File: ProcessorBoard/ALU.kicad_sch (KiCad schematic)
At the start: 2 parts, among them U43 IDT7381

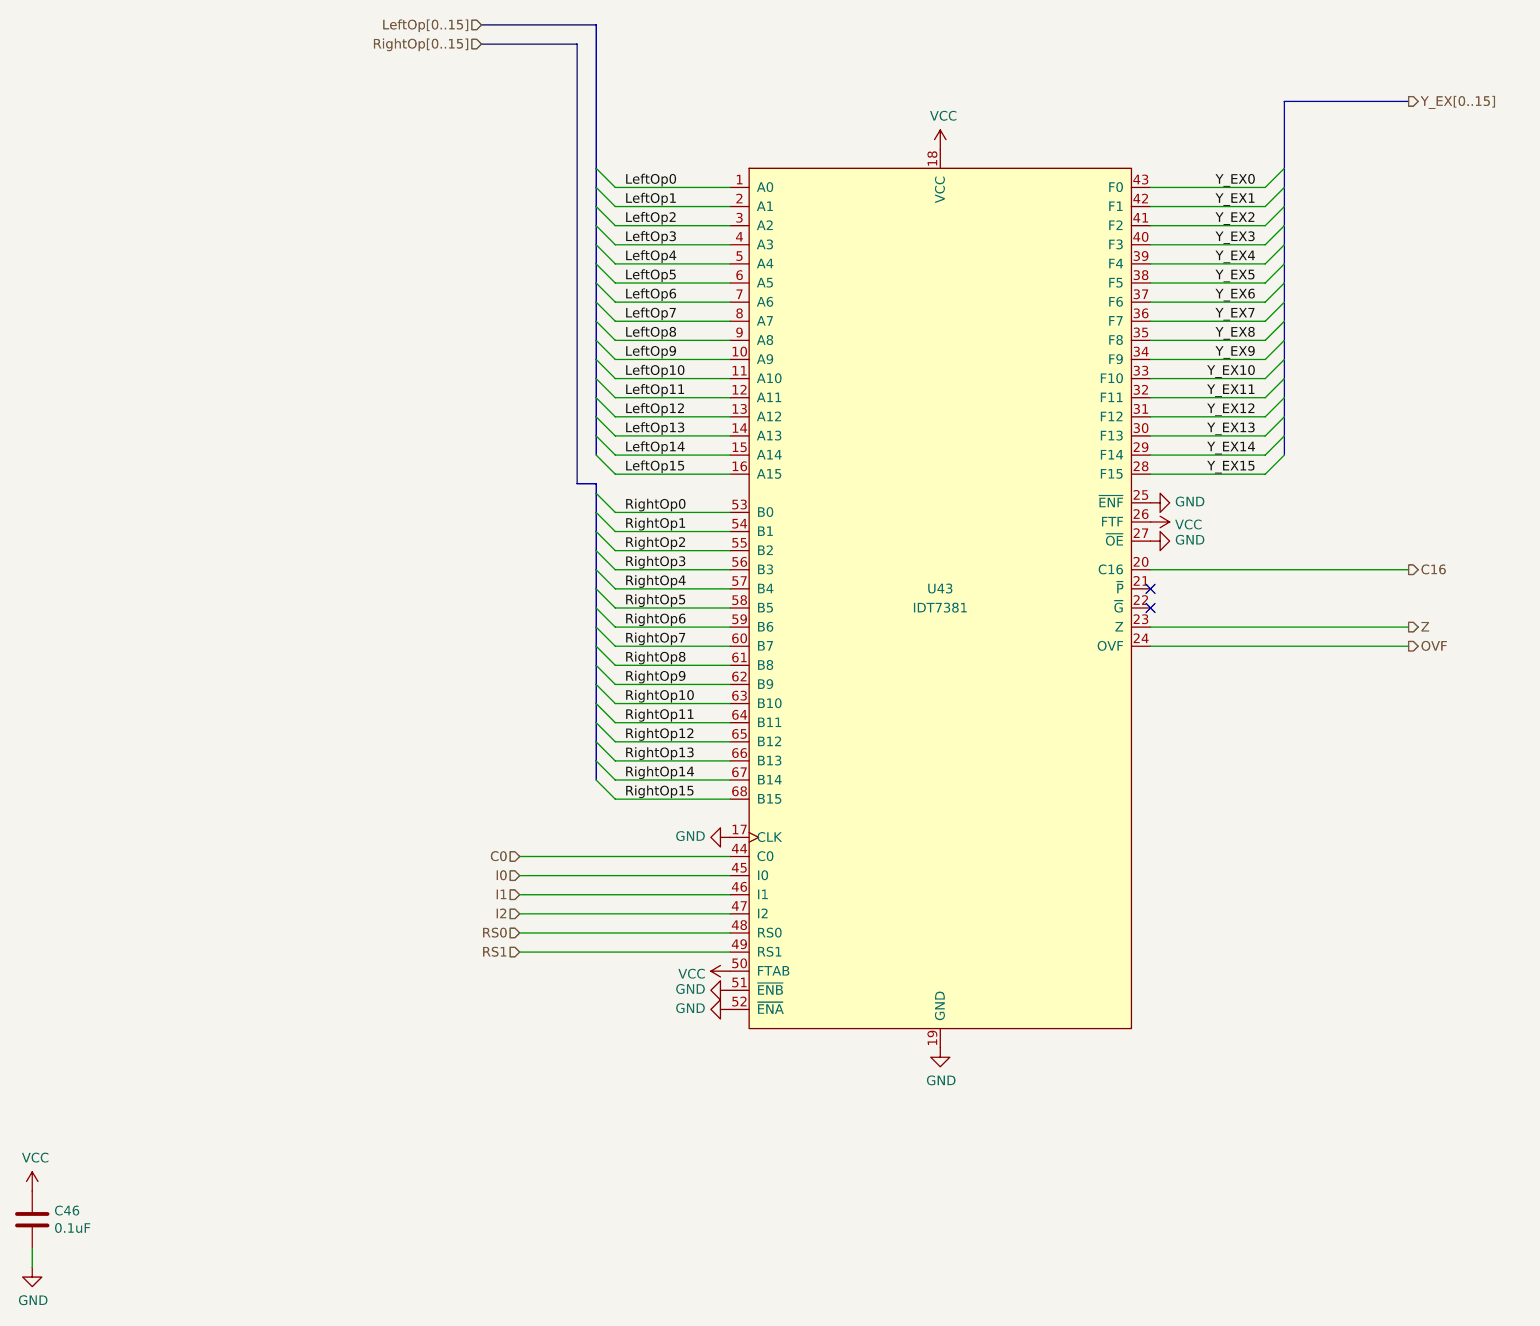
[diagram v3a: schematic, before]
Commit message: ProcessorBoard: Replace Instruction ROM with a header for a daughter board
ROMs will be relocated to a daughter board to allow the memories and their
sockets to be swapped easily.
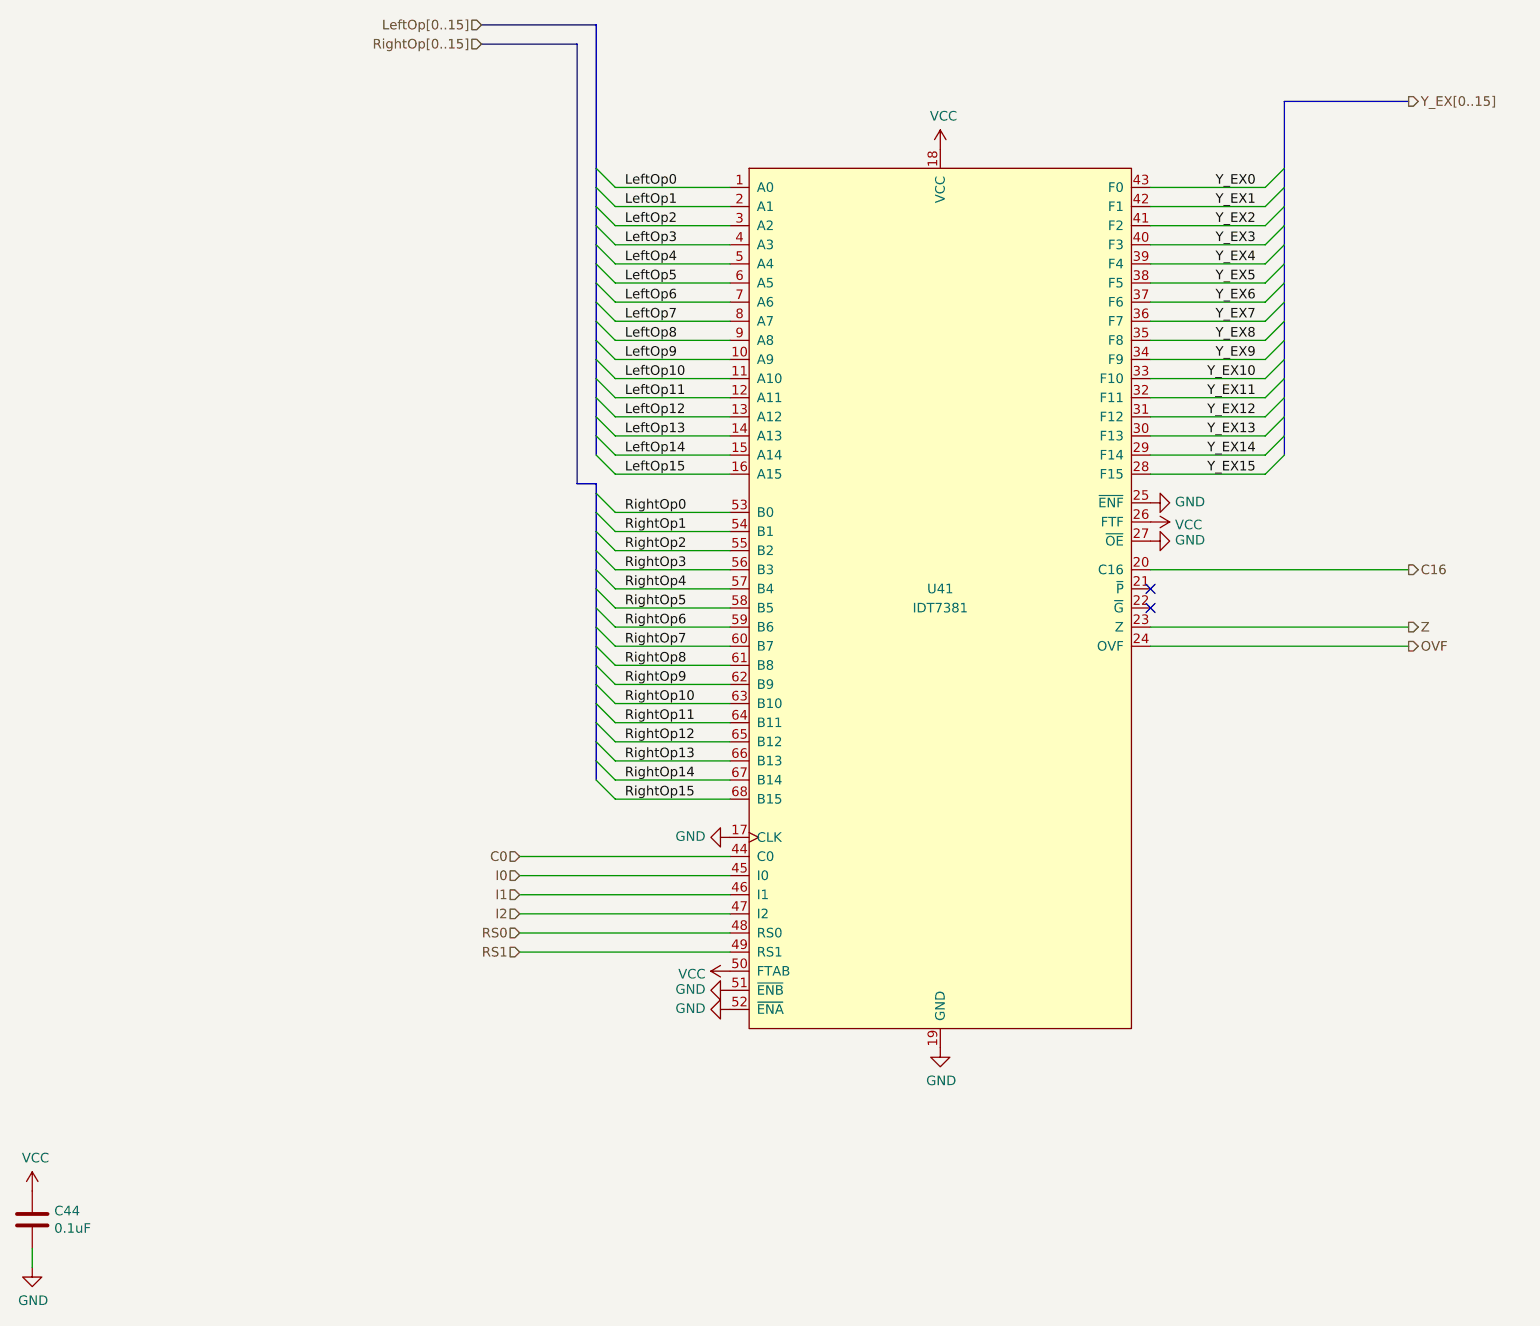
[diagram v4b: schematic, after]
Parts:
- renumbered C46 to C44, U43 to U41
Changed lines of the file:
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@@
   (symbol (lib_id "Device:C") (at 21.59 185.42 0) (unit 1)
     (in_bom yes) (on_board yes) (dnp no)
-    (property "Reference" "C46" (at 24.511 184.2516 0)
+    (property "Reference" "C44" (at 24.511 184.2516 0)
       (effects (font (size 1.27 1.27)) (justify left))
     )
@@
       (project "ProcessorBoard"
         (path "/83c5181e-f5ee-453c-ae5c-d7256ba8837d/00000000-0000-0000-0000-000060a71bbf/00000000-0000-0000-0000-00005fc6fe4b"
-          (reference "C46") (unit 1)
+          (reference "C44") (unit 1)
         )
       )
@@
   (symbol (lib_id "power:VCC") (at 21.59 181.61 0) (unit 1)
     (in_bom yes) (on_board yes) (dnp no)
-    (property "Reference" "#PWR0293" (at 21.59 185.42 0)
+    (property "Reference" "#PWR0285" (at 21.59 185.42 0)
       (effects (font (size 1.27 1.27)) hide)
     )
@@
       (project "ProcessorBoard"
         (path "/83c5181e-f5ee-453c-ae5c-d7256ba8837d/00000000-0000-0000-0000-000060a71bbf/00000000-0000-0000-0000-00005fc6fe4b"
-          (reference "#PWR0293") (unit 1)
+          (reference "#PWR0285") (unit 1)
         )
       )
@@
   (symbol (lib_id "power:GND") (at 21.59 191.77 0) (unit 1)
     (in_bom yes) (on_board yes) (dnp no)
-    (property "Reference" "#PWR0294" (at 21.59 198.12 0)
+    (property "Reference" "#PWR0286" (at 21.59 198.12 0)
       (effects (font (size 1.27 1.27)) hide)
     )
@@
       (project "ProcessorBoard"
         (path "/83c5181e-f5ee-453c-ae5c-d7256ba8837d/00000000-0000-0000-0000-000060a71bbf/00000000-0000-0000-0000-00005fc6fe4b"
-          (reference "#PWR0294") (unit 1)
+          (reference "#PWR0286") (unit 1)
         )
       )
@@
   (symbol (lib_id "EXModule-rescue:IDT7381-CPU") (at 142.24 102.87 0) (unit 1)
     (in_bom yes) (on_board yes) (dnp no)
-    (property "Reference" "U43" (at 142.24 101.6 0)
+    (property "Reference" "U41" (at 142.24 101.6 0)
       (effects (font (size 1.27 1.27)))
     )
@@
       (project "ProcessorBoard"
         (path "/83c5181e-f5ee-453c-ae5c-d7256ba8837d/00000000-0000-0000-0000-000060a71bbf/00000000-0000-0000-0000-00005fc6fe4b"
-          (reference "U43") (unit 1)
+          (reference "U41") (unit 1)
         )
       )
@@
   (symbol (lib_id "power:VCC") (at 142.24 43.18 0) (unit 1)
     (in_bom yes) (on_board yes) (dnp no)
-    (property "Reference" "#PWR0299" (at 142.24 46.99 0)
+    (property "Reference" "#PWR0291" (at 142.24 46.99 0)
       (effects (font (size 1.27 1.27)) hide)
     )
@@
       (project "ProcessorBoard"
         (path "/83c5181e-f5ee-453c-ae5c-d7256ba8837d/00000000-0000-0000-0000-000060a71bbf/00000000-0000-0000-0000-00005fc6fe4b"
-          (reference "#PWR0299") (unit 1)
+          (reference "#PWR0291") (unit 1)
         )
       )
@@
   (symbol (lib_id "power:GND") (at 142.24 162.56 0) (unit 1)
     (in_bom yes) (on_board yes) (dnp no)
-    (property "Reference" "#PWR0300" (at 142.24 168.91 0)
+    (property "Reference" "#PWR0292" (at 142.24 168.91 0)
       (effects (font (size 1.27 1.27)) hide)
     )
@@
       (project "ProcessorBoard"
         (path "/83c5181e-f5ee-453c-ae5c-d7256ba8837d/00000000-0000-0000-0000-000060a71bbf/00000000-0000-0000-0000-00005fc6fe4b"
-          (reference "#PWR0300") (unit 1)
+          (reference "#PWR0292") (unit 1)
         )
       )
@@
   (symbol (lib_id "power:GND") (at 170.18 90.17 90) (unit 1)
     (in_bom yes) (on_board yes) (dnp no)
-    (property "Reference" "#PWR0301" (at 176.53 90.17 0)
+    (property "Reference" "#PWR0293" (at 176.53 90.17 0)
       (effects (font (size 1.27 1.27)) hide)
     )
@@
       (project "ProcessorBoard"
         (path "/83c5181e-f5ee-453c-ae5c-d7256ba8837d/00000000-0000-0000-0000-000060a71bbf/00000000-0000-0000-0000-00005fc6fe4b"
-          (reference "#PWR0301") (unit 1)
+          (reference "#PWR0293") (unit 1)
         )
       )
@@
   (symbol (lib_id "power:GND") (at 114.3 154.94 270) (mirror x) (unit 1)
     (in_bom yes) (on_board yes) (dnp no)
-    (property "Reference" "#PWR0297" (at 107.95 154.94 0)
+    (property "Reference" "#PWR0289" (at 107.95 154.94 0)
       (effects (font (size 1.27 1.27)) hide)
     )
@@
       (project "ProcessorBoard"
         (path "/83c5181e-f5ee-453c-ae5c-d7256ba8837d/00000000-0000-0000-0000-000060a71bbf/00000000-0000-0000-0000-00005fc6fe4b"
-          (reference "#PWR0297") (unit 1)
+          (reference "#PWR0289") (unit 1)
         )
       )
@@
   (symbol (lib_id "power:GND") (at 114.3 157.48 270) (mirror x) (unit 1)
     (in_bom yes) (on_board yes) (dnp no)
-    (property "Reference" "#PWR0298" (at 107.95 157.48 0)
+    (property "Reference" "#PWR0290" (at 107.95 157.48 0)
       (effects (font (size 1.27 1.27)) hide)
     )
@@
       (project "ProcessorBoard"
         (path "/83c5181e-f5ee-453c-ae5c-d7256ba8837d/00000000-0000-0000-0000-000060a71bbf/00000000-0000-0000-0000-00005fc6fe4b"
-          (reference "#PWR0298") (unit 1)
+          (reference "#PWR0290") (unit 1)
         )
       )
@@
   (symbol (lib_id "power:VCC") (at 170.18 92.71 270) (unit 1)
     (in_bom yes) (on_board yes) (dnp no)
-    (property "Reference" "#PWR0302" (at 166.37 92.71 0)
+    (property "Reference" "#PWR0294" (at 166.37 92.71 0)
       (effects (font (size 1.27 1.27)) hide)
     )
@@
       (project "ProcessorBoard"
         (path "/83c5181e-f5ee-453c-ae5c-d7256ba8837d/00000000-0000-0000-0000-000060a71bbf/00000000-0000-0000-0000-00005fc6fe4b"
-          (reference "#PWR0302") (unit 1)
+          (reference "#PWR0294") (unit 1)
         )
       )
@@
   (symbol (lib_id "power:GND") (at 114.3 134.62 270) (mirror x) (unit 1)
     (in_bom yes) (on_board yes) (dnp no)
-    (property "Reference" "#PWR0295" (at 107.95 134.62 0)
+    (property "Reference" "#PWR0287" (at 107.95 134.62 0)
       (effects (font (size 1.27 1.27)) hide)
     )
@@
       (project "ProcessorBoard"
         (path "/83c5181e-f5ee-453c-ae5c-d7256ba8837d/00000000-0000-0000-0000-000060a71bbf/00000000-0000-0000-0000-00005fc6fe4b"
-          (reference "#PWR0295") (unit 1)
+          (reference "#PWR0287") (unit 1)
         )
       )
@@
   (symbol (lib_id "power:VCC") (at 114.3 152.4 90) (mirror x) (unit 1)
     (in_bom yes) (on_board yes) (dnp no)
-    (property "Reference" "#PWR0296" (at 118.11 152.4 0)
+    (property "Reference" "#PWR0288" (at 118.11 152.4 0)
       (effects (font (size 1.27 1.27)) hide)
     )
@@
       (project "ProcessorBoard"
         (path "/83c5181e-f5ee-453c-ae5c-d7256ba8837d/00000000-0000-0000-0000-000060a71bbf/00000000-0000-0000-0000-00005fc6fe4b"
-          (reference "#PWR0296") (unit 1)
+          (reference "#PWR0288") (unit 1)
         )
       )
@@
   (symbol (lib_id "power:GND") (at 170.18 95.25 90) (unit 1)
     (in_bom yes) (on_board yes) (dnp no)
-    (property "Reference" "#PWR0303" (at 176.53 95.25 0)
+    (property "Reference" "#PWR0295" (at 176.53 95.25 0)
       (effects (font (size 1.27 1.27)) hide)
     )
@@
       (project "ProcessorBoard"
         (path "/83c5181e-f5ee-453c-ae5c-d7256ba8837d/00000000-0000-0000-0000-000060a71bbf/00000000-0000-0000-0000-00005fc6fe4b"
-          (reference "#PWR0303") (unit 1)
-        )
-      )
+          (reference "#PWR0295") (unit 1)
+        )
+      )

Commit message: ProcessorBoard: Copy symbols into project symbol library, make consistent
Symbols created for Turtle16 have been copied into a project-specific
symbol library. The symbols have all been updated with manufacturer,
manufacturer part number, mouser part number, and digikey part number.

Test points and mounting holes have been marked to be excluded from BOM.
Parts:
- C44: footprint Capacitor_SMD:C_0603_1608Metric_Pad1.08x0.95mm_HandSolder -> Capacitor_SMD:C_0603_1608Metric; Digikey# (none) -> 587-6004-1-ND; Manufacturer (none) -> Taiyo Yuden; Manufacturer# (none) -> EMK107B7104KAHT; Mouser https://www.mouser.com/ProductDetail/963-EMK107B7104KAHT -> (none); Mouser# (none) -> 963-EMK107B7104KAHT
- U41: symbol EXModule-rescue:IDT7381-CPU -> Turtle16:IDT7381; Digikey# (none) -> 3M6821B1-ND; Manufacturer (none) -> 3M; Manufacturer# (none) -> 8468-21B1-RK-TP; Mouser https://www.mouser.com/ProductDetail/3M-Electronic-Solution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 -> (none); Mouser# (none) -> 517-8468-21B1-RK-TP
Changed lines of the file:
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@@
   (title_block
     (title "ALU")
-    (date "2023-11-20")
+    (date "2023-11-25")
     (rev "A")
     (comment 2 "are latched in registers in other parts of the circuit.")
@@
       (effects (font (size 1.27 1.27)) (justify left))
     )
-    (property "Footprint" "Capacitor_SMD:C_0603_1608Metric_Pad1.08x0.95mm_HandSolder" (at 22.5552 189.23 0)
-      (effects (font (size 1.27 1.27)) hide)
-    )
-    (property "Datasheet" "~" (at 21.59 185.42 0)
-      (effects (font (size 1.27 1.27)) hide)
-    )
-    (property "Mouser" "https://www.mouser.com/ProductDetail/963-EMK107B7104KAHT" (at 21.59 185.42 0)
+    (property "Footprint" "Capacitor_SMD:C_0603_1608Metric" (at 128.5748 82.55 0)
+      (effects (font (size 1.27 1.27)) hide)
+    )
+    (property "Datasheet" "https://www.mouser.com/datasheet/2/396/taiyo_yuden_12132018_mlcc11_hq_e-1510082.pdf" (at 129.54 78.74 0)
+      (effects (font (size 1.27 1.27)) hide)
+    )
+    (property "Manufacturer" "Taiyo Yuden" (at 129.54 78.74 0)
+      (effects (font (size 1.27 1.27)) hide)
+    )
+    (property "Manufacturer#" "EMK107B7104KAHT" (at 129.54 78.74 0)
+      (effects (font (size 1.27 1.27)) hide)
+    )
+    (property "Mouser#" "963-EMK107B7104KAHT" (at 129.54 78.74 0)
+      (effects (font (size 1.27 1.27)) hide)
+    )
+    (property "Digikey#" "587-6004-1-ND" (at 129.54 78.74 0)
       (effects (font (size 1.27 1.27)) hide)
     )
@@
     )
   )
-  (symbol (lib_id "EXModule-rescue:IDT7381-CPU") (at 142.24 102.87 0) (unit 1)
+  (symbol (lib_id "Turtle16:IDT7381") (at 142.24 102.87 0) (unit 1)
     (in_bom yes) (on_board yes) (dnp no)
     (property "Reference" "U41" (at 142.24 101.6 0)
@@
       (effects (font (size 1.27 1.27)) hide)
     )
-    (property "Datasheet" "https://www.digchip.com/datasheets/download_datasheet.php?id=419696&part-number=IDT7381" (at 142.24 71.12 0)
-      (effects (font (size 1.27 1.27)) hide)
-    )
-    (property "Mouser" "https://www.mouser.com/ProductDetail/3M-Electronic-Solutions-Division/8468-21B1-RK-TP?qs=WZRMhwwaLl%2FJN6Bcf7US3Q%3D%3D" (at 142.24 102.87 0)
-      (effects (font (size 1.27 1.27)) hide)
-    )
+    (property "Datasheet" "https://www.mouser.com/datasheet/2/1/62074255ead63bd7ee299038194cccf20f500ef4-2950939.pdf" (at 142.24 71.12 0)
+      (effects (font (size 1.27 1.27)) hide)
+    )
+    (property "Manufacturer" "3M" (at 142.24 102.87 0)
+      (effects (font (size 1.27 1.27)) hide)
+    )
+    (property "Manufacturer#" "8468-21B1-RK-TP" (at 142.24 102.87 0)
+      (effects (font (size 1.27 1.27)) hide)
+    )
+    (property "Mouser#" "517-8468-21B1-RK-TP" (at 142.24 102.87 0)
+      (effects (font (size 1.27 1.27)) hide)
+    )
+    (property "Digikey#" "3M6821B1-ND" (at 142.24 102.87 0)
+      (effects (font (size 1.27 1.27)) hide)
+    )
